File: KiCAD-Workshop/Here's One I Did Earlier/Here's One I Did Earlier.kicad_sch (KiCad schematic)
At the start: 28 parts, among them J1 Screw Terminal, J2 Debug Header, J3 UART Header, Q1 AO3401A, Q2 AO3400A, U1 STM8S003F3U, U2 MS5607-02BA, U3 W25Q128JVS, U4 AMS1117-3.3

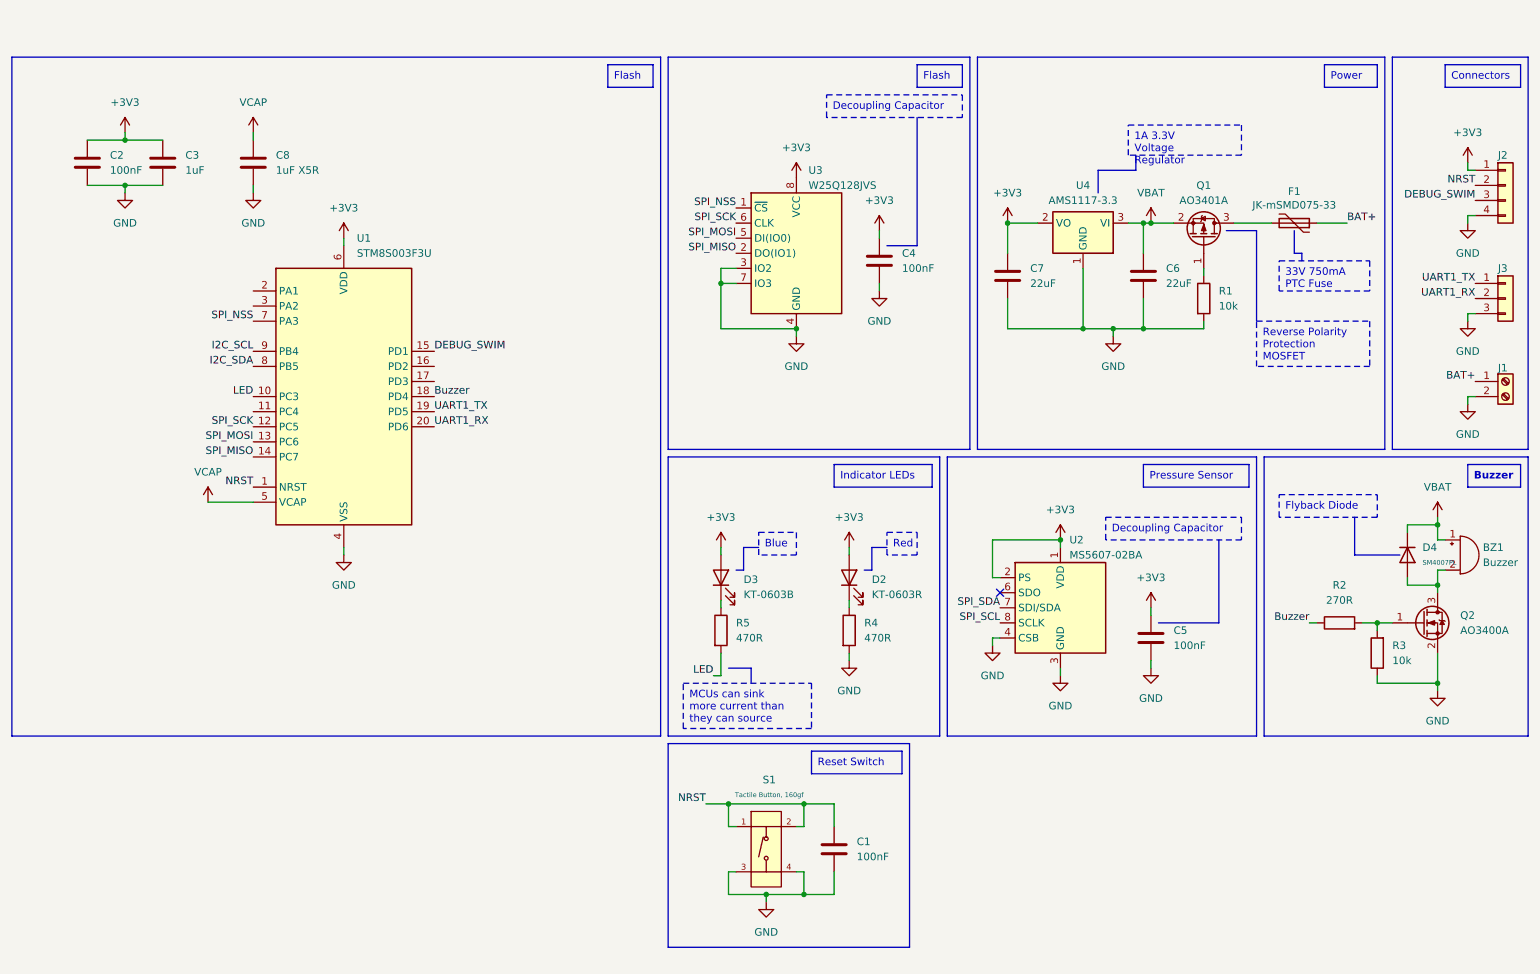
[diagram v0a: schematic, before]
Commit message: Fnished Example PCB
Routed PCB
Fixed many DRC
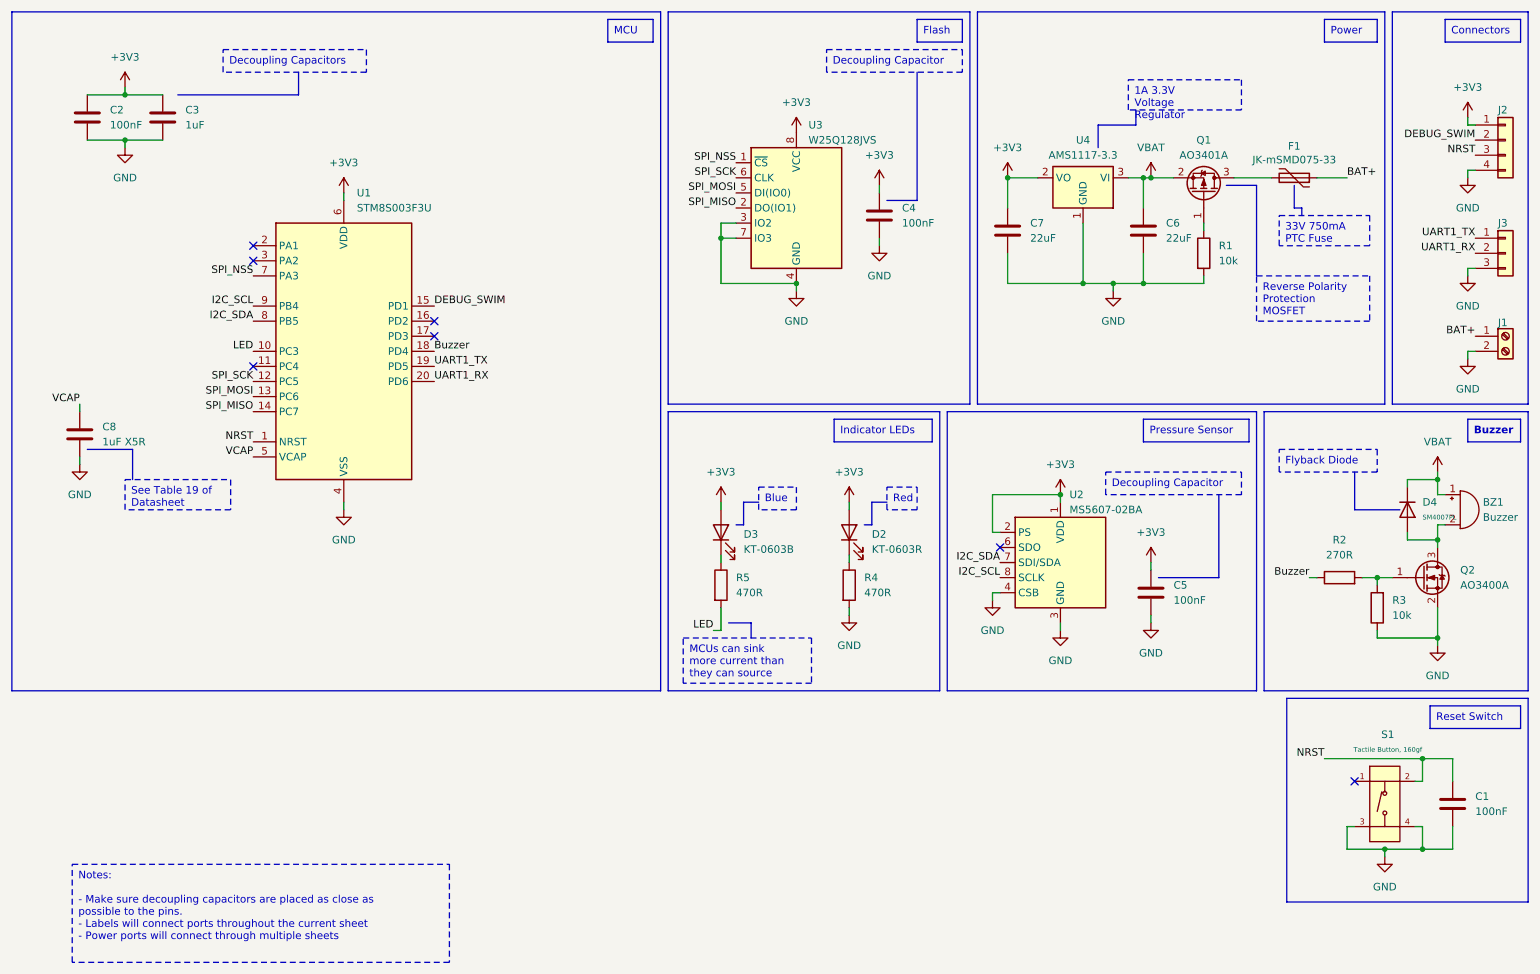
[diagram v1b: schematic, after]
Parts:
- BZ1: footprint (none) -> Buzzer_Beeper:MagneticBuzzer_Kingstate_KCG0601
- C1, C2, C3, C4, C5, C6, C7, C8: footprint (none) -> Capacitor_SMD:C_0603_1608Metric
- J2: footprint (none) -> Connector_PinHeader_2.54mm:PinHeader_1x04_P2.54mm_Vertical
- J3: footprint (none) -> Connector_PinHeader_1.00mm:PinHeader_1x03_P1.00mm_Vertical
- R1, R2, R3, R4, R5: footprint (none) -> Resistor_SMD:R_0603_1608Metric
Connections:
- net SPI_SCL is gone; now on net I2C_SCL: U2.8 (SCLK)
- net SPI_SDA is gone; now on net I2C_SDA: U2.7 (SDI/SDA)
- net DEBUG_SWIM: now also J2.2 (Pin_2); no longer J2.3 (Pin_3)
- net NRST: now also J2.3 (Pin_3); no longer J2.2 (Pin_2), S1.1 (A)
- no-connect marks 1 -> 7
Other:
- moved on the sheet: BZ1, C1, C2, C3, C4, C5, C6, C7, C8, D2, D3, D4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
